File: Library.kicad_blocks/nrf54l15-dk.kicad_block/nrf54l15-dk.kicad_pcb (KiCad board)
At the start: 2 copper layers, 13 parts, among them J1 Conn_02x02_Odd_Even, J2 Conn_02x02_Odd_Even, J3 Conn_02x02_Odd_Even, J4 Conn_02x10_Odd_Even, J5 Conn_02x10_Odd_Even, J6 Conn_02x10_Odd_Even

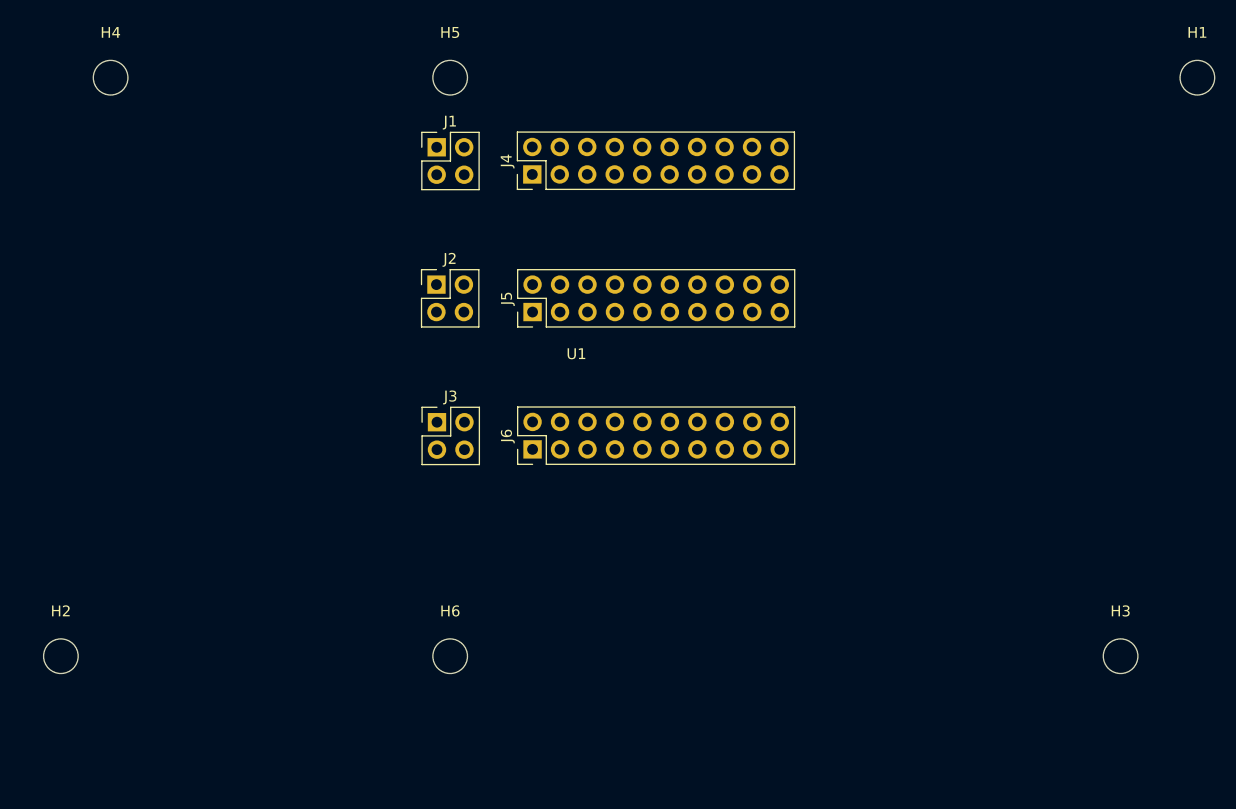
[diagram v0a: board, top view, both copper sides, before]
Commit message: starting point of design block
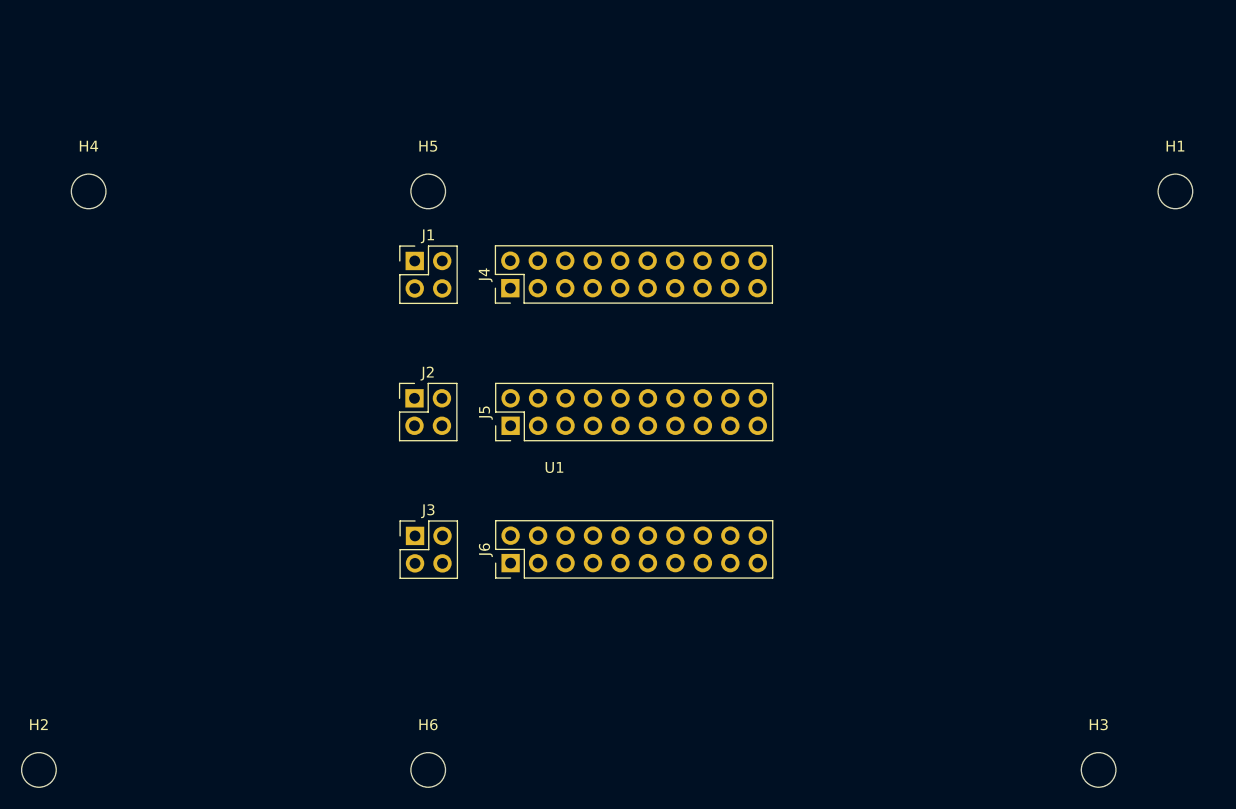
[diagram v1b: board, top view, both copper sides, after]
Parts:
- moved H4 10.7 mm to (42.4, 46.9)
- moved U1 10.7 mm to (42.4, 46.9)
- moved H2 10.7 mm to (37.8, 100.4)
- moved H5 10.7 mm to (73.8, 46.9)
- moved H6 10.7 mm to (73.8, 100.4)
- moved J3 10.7 mm to (72.6, 78.7)
- moved J5 10.7 mm to (81.5, 68.5)
- moved J6 10.7 mm to (81.5, 81.2)
- moved H3 10.7 mm to (135.8, 100.4)
- moved H1 10.7 mm to (142.9, 46.9)
- moved J1 10.7 mm to (72.6, 53.3)
- moved J2 10.7 mm to (72.6, 66.0)
- moved J4 10.7 mm to (81.4, 55.8)
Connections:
- net /P0.00 renamed /nrf54l15-dk/P0.00
- net /P0.01 renamed /nrf54l15-dk/P0.01
- net /P0.02 renamed /nrf54l15-dk/P0.02
- net /P0.03 renamed /nrf54l15-dk/P0.03
- net /P0.04 renamed /nrf54l15-dk/P0.04
- net /P1.00 renamed /nrf54l15-dk/P1.00
- net /P1.01 renamed /nrf54l15-dk/P1.01
- net /P1.02 renamed /nrf54l15-dk/P1.02
- net /P1.03 renamed /nrf54l15-dk/P1.03
- net /P1.04 renamed /nrf54l15-dk/P1.04
- net /P1.05 renamed /nrf54l15-dk/P1.05
- net /P1.06 renamed /nrf54l15-dk/P1.06
- net /P1.07 renamed /nrf54l15-dk/P1.07
- net /P1.08 renamed /nrf54l15-dk/P1.08
- net /P1.09 renamed /nrf54l15-dk/P1.09
- net /P1.10 renamed /nrf54l15-dk/P1.10
- net /P1.11 renamed /nrf54l15-dk/P1.11
- net /P1.12 renamed /nrf54l15-dk/P1.12
- net /P1.13 renamed /nrf54l15-dk/P1.13
- net /P1.14 renamed /nrf54l15-dk/P1.14
- net /P2.00 renamed /nrf54l15-dk/P2.00
- net /P2.01 renamed /nrf54l15-dk/P2.01
- net /P2.02 renamed /nrf54l15-dk/P2.02
- net /P2.03 renamed /nrf54l15-dk/P2.03
- net /P2.04 renamed /nrf54l15-dk/P2.04
- net /P2.05 renamed /nrf54l15-dk/P2.05
- net /P2.06 renamed /nrf54l15-dk/P2.06
- net /P2.07 renamed /nrf54l15-dk/P2.07
- net /P2.08 renamed /nrf54l15-dk/P2.08
- net /P2.09 renamed /nrf54l15-dk/P2.09
- net /P2.10 renamed /nrf54l15-dk/P2.10

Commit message: [fab] complete the design of semtech dev board
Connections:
- J1 pad 1: +5V -> GND
- J1 pad 3: unconnected-(J1-Pin_3-Pad3) -> +5V
- J1 pad 4: GND -> unconnected-(J1-Pin_4-Pad4)
- J2 pad 1: +5V -> GND
- J2 pad 3: unconnected-(J2-Pin_3-Pad3) -> +5V
- J2 pad 4: GND -> unconnected-(J2-Pin_4-Pad4)
- J3 pad 1: +5V -> GND
- J3 pad 3: unconnected-(J3-Pin_3-Pad3) -> +5V
- J3 pad 4: GND -> unconnected-(J3-Pin_4-Pad4)
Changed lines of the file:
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@@
 			(layers "*.Cu" "*.Mask")
 			(remove_unused_layers no)
-			(net "+5V")
+			(net "GND")
 			(pinfunction "GND_1")
 			(pintype "passive")
@@
 			(layers "*.Cu" "*.Mask")
 			(remove_unused_layers no)
-			(net "unconnected-(J1-Pin_3-Pad3)")
+			(net "+5V")
 			(pinfunction "Pin_3_3")
-			(pintype "passive+no_connect")
+			(pintype "passive")
 		)
 		(pad "4" thru_hole circle
@@
 			(layers "*.Cu" "*.Mask")
 			(remove_unused_layers no)
-			(net "GND")
+			(net "unconnected-(J1-Pin_4-Pad4)")
 			(pinfunction "Pin_4_4")
-			(pintype "passive")
+			(pintype "passive+no_connect")
 		)
 		(embedded_fonts no)
@@
 			(layers "*.Cu" "*.Mask")
 			(remove_unused_layers no)
-			(net "+5V")
+			(net "GND")
 			(pinfunction "Pin_1_1")
 			(pintype "passive")
@@
 			(layers "*.Cu" "*.Mask")
 			(remove_unused_layers no)
-			(net "unconnected-(J2-Pin_3-Pad3)")
+			(net "+5V")
 			(pinfunction "Pin_3_3")
-			(pintype "passive+no_connect")
+			(pintype "passive")
 		)
 		(pad "4" thru_hole circle
@@
 			(layers "*.Cu" "*.Mask")
 			(remove_unused_layers no)
-			(net "GND")
+			(net "unconnected-(J2-Pin_4-Pad4)")
 			(pinfunction "Pin_4_4")
-			(pintype "passive")
+			(pintype "passive+no_connect")
 		)
 		(embedded_fonts no)
@@
 		(at 42.4374 46.8554)
 		(property "Reference" "U1"
-			(at 43.08 25.56 0)
+			(at 0 -1.5 0)
 			(unlocked yes)
 			(layer "F.SilkS")
@@
 		)
 		(property "Value" "~"
-			(at 43.08 27.06 0)
+			(at 0 0 0)
 			(unlocked yes)
 			(layer "F.Fab")
@@
 		)
 		(fp_text user "${REFERENCE}"
-			(at 43.08 28.56 0)
+			(at 0 1.5 0)
 			(unlocked yes)
 			(layer "F.Fab")
@@
 			(layers "*.Cu" "*.Mask")
 			(remove_unused_layers no)
-			(net "+5V")
+			(net "GND")
 			(pinfunction "Pin_1_1")
 			(pintype "passive")
@@
 			(layers "*.Cu" "*.Mask")
 			(remove_unused_layers no)
-			(net "unconnected-(J3-Pin_3-Pad3)")
+			(net "+5V")
 			(pinfunction "Pin_3_3")
-			(pintype "passive+no_connect")
+			(pintype "passive")
 		)
 		(pad "4" thru_hole circle
@@
 			(layers "*.Cu" "*.Mask")
 			(remove_unused_layers no)
-			(net "GND")
+			(net "unconnected-(J3-Pin_4-Pad4)")
 			(pinfunction "Pin_4_4")
-			(pintype "passive")
+			(pintype "passive+no_connect")
 		)
 		(embedded_fonts no)
